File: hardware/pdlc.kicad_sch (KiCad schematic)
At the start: 10 parts, among them J1 TBP01R1-508-06BE

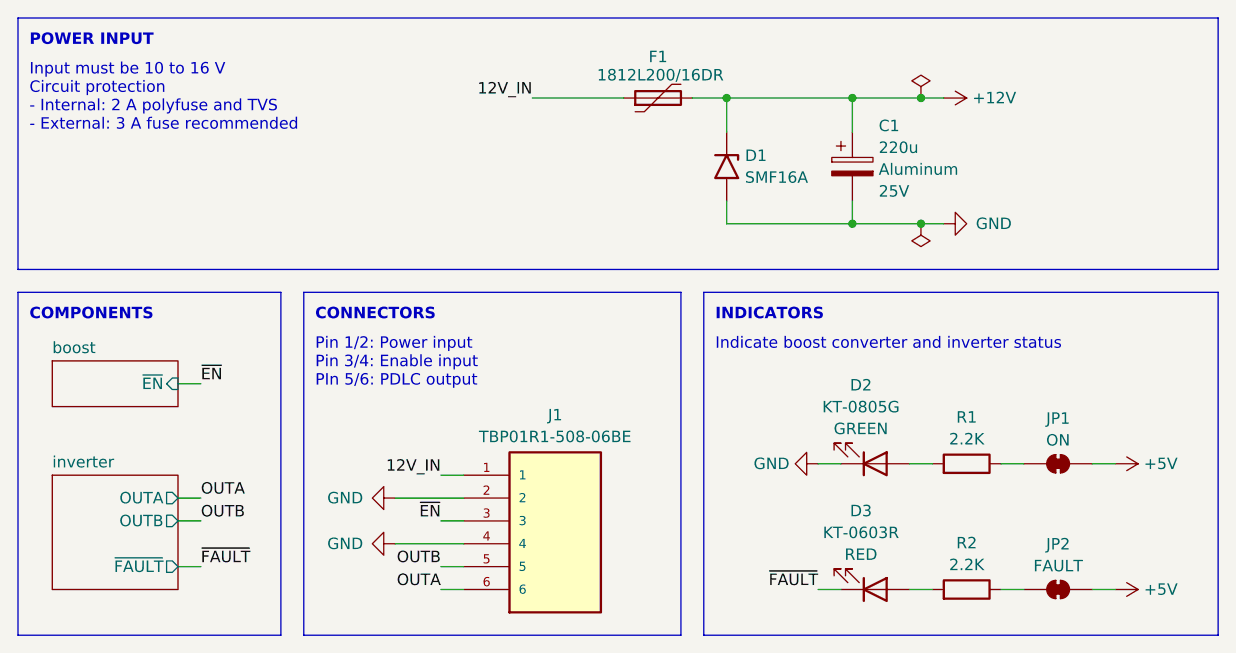
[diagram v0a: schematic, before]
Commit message: Revised layout using LM5108 and discrete FETs
LM5108 is less expensive but it requires more board area.  In lieu of
active current limiting, we rely on the LM5158 hiccup overload
protection.  The FETs are intentionally oversized to handle large
current pulses when switching the polarity of the capacitive load.

This design is complete and ready for manufacture.
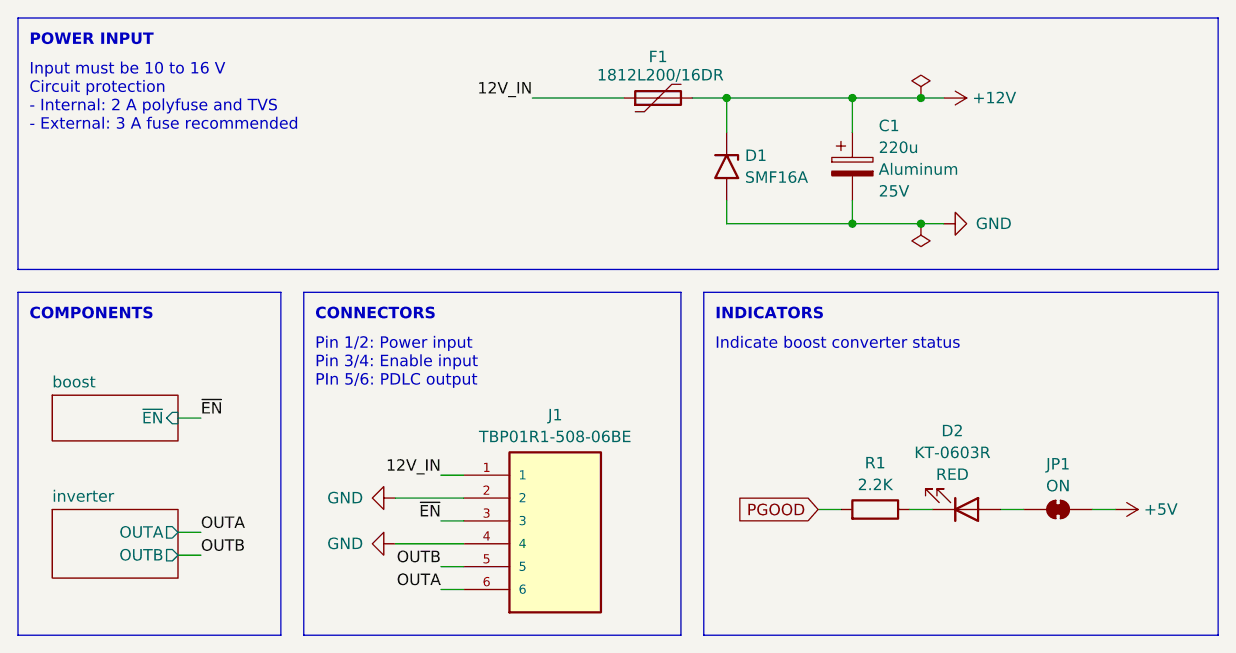
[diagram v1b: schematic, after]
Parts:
- removed D3: KT-0603R, LED_SMD:LED_0603_1608Metric, symbol Device:LED
- removed JP2: SolderJumper_2_Bridged, Jumper:SolderJumper-2_P1.3mm_Bridged_RoundedPad1.0x1.5mm, symbol Jumper:SolderJumper_2_Bridged
- removed R2: 2.2K, Resistor_SMD:R_0603_1608Metric, symbol Device:R
- D2: value KT-0805G -> KT-0603R; footprint LED_SMD:LED_0805_2012Metric -> LED_SMD:LED_0603_1608Metric_Pad1.05x0.95mm_HandSolder; LCSC C2297 -> C2286; Rating GREEN -> RED
- F1: footprint Fuse:Fuse_1812_4532Metric -> 1812L:1812L
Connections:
- net GND: no longer D2.1 (K)
- net at R1.1: now also D2.1 (K); no longer JP1.2 (B)
- net at D2.2 (A): now also JP1.2 (B); no longer R1.2
- new net PGOOD: R1.2
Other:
- sheet inverter ports: added none; removed ~{FAULT}
- note added: "Indicate boost converter status"
- note removed: "Indicate boost converter and inverter status"
- moved on the sheet: D2, JP1, R1
